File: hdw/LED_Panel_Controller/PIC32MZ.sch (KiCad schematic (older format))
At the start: 3 parts

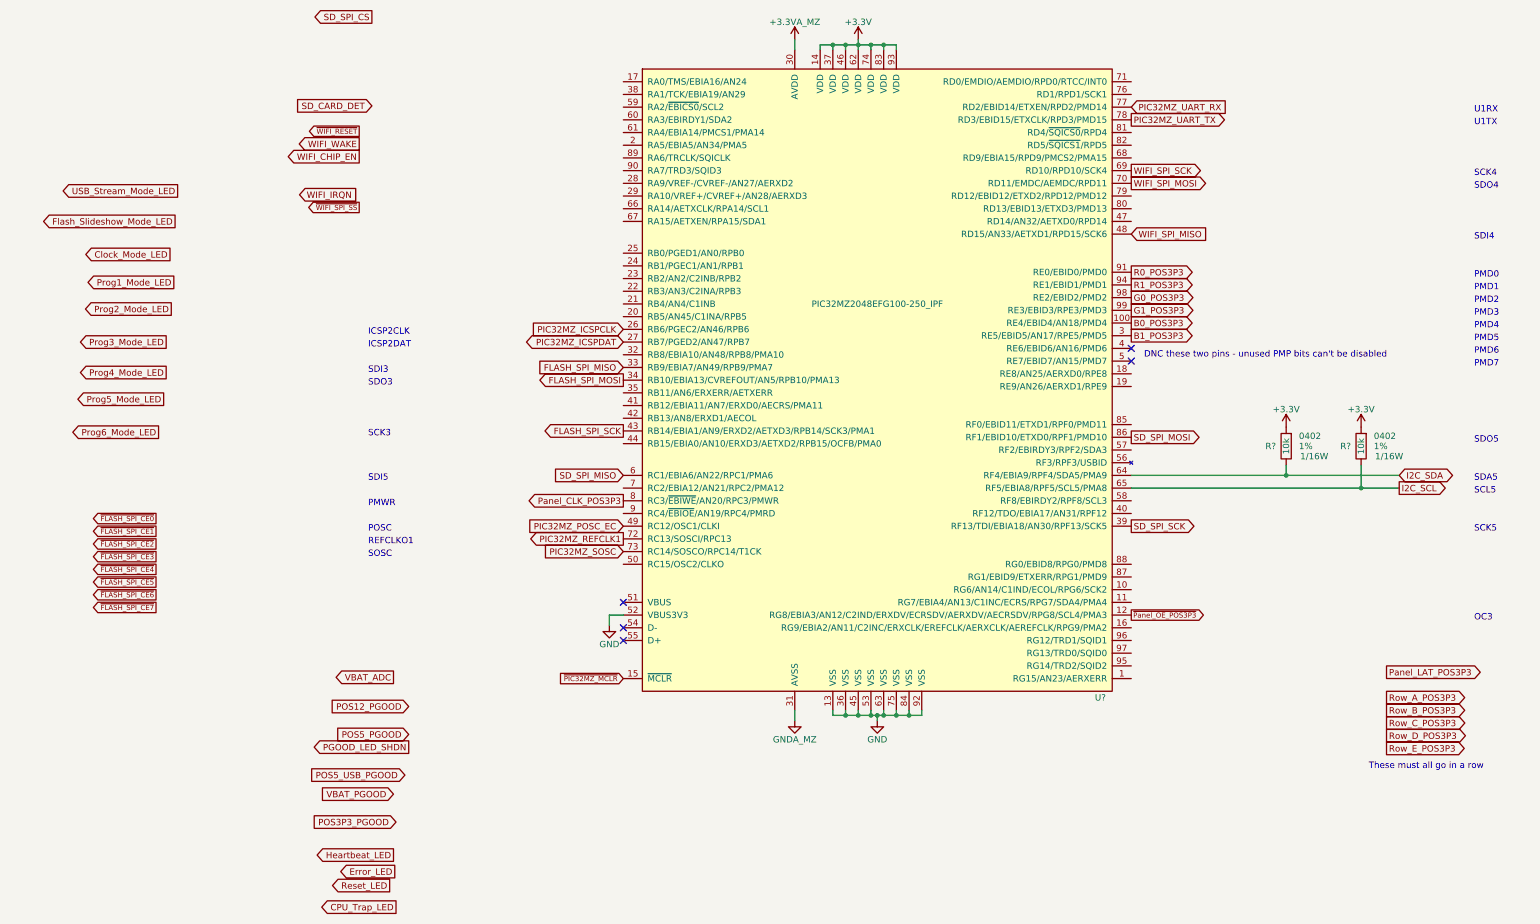
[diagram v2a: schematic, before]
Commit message: assigned a lot of nets to MCU pins
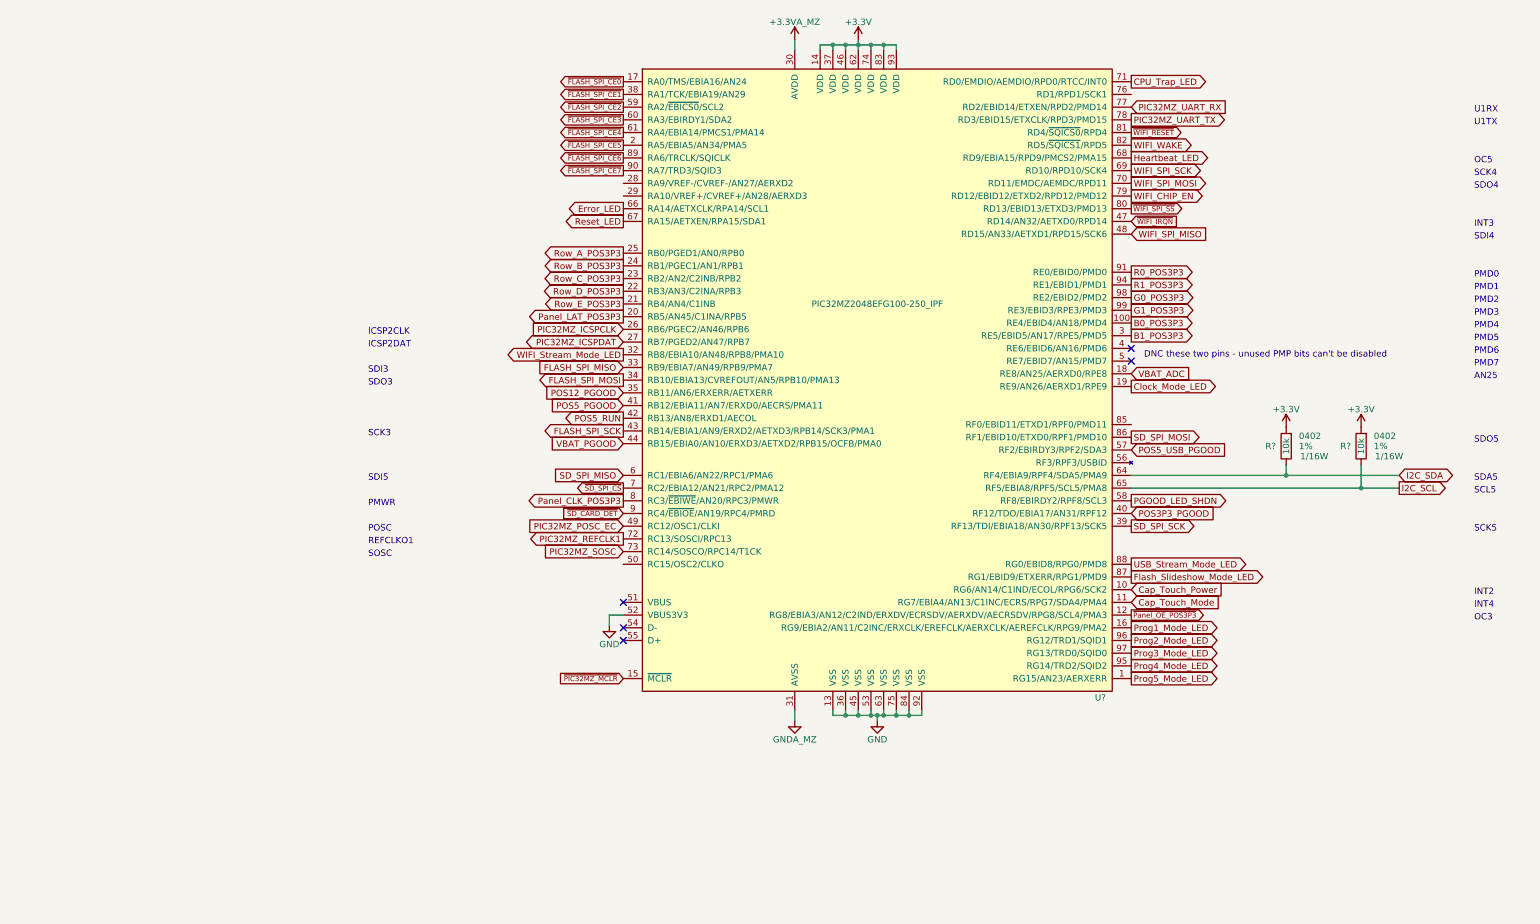
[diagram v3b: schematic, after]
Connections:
- net CPU_Trap_LED: now also U?.71 (RD0/EMDIO/AEMDIO/RPD0/RTCC/INT0)
- net Clock_Mode_LED: now also U?.19 (RE9/AN26/AERXD1/RPE9)
- net Error_LED: now also U?.66 (RA14/AETXCLK/RPA14/SCL1)
- net Flash_Slideshow_Mode_LED: now also U?.87 (RG1/EBID9/ETXERR/RPG1/PMD9)
- net Heartbeat_LED: now also U?.68 (RD9/EBIA15/RPD9/PMCS2/PMA15)
- net PGOOD_LED_SHDN: now also U?.58 (RF8/EBIRDY2/RPF8/SCL3)
- net POS12_PGOOD: now also U?.35 (RB11/AN6/ERXERR/AETXERR)
- net POS3P3_PGOOD: now also U?.40 (RF12/TDO/EBIA17/AN31/RPF12)
- net POS5_PGOOD: now also U?.41 (RB12/EBIA11/AN7/ERXD0/AECRS/PMA11)
- net POS5_USB_PGOOD: now also U?.57 (RF2/EBIRDY3/RPF2/SDA3)
- net Panel_LAT_POS3P3: now also U?.20 (RB5/AN45/C1INA/RPB5)
- net Prog1_Mode_LED: now also U?.16 (RG9/EBIA2/AN11/C2INC/ERXCLK/EREFCLK/AERXCLK/AEREFCLK/RPG9/PMA2)
- net Prog2_Mode_LED: now also U?.96 (RG12/TRD1/SQID1)
- net Prog3_Mode_LED: now also U?.97 (RG13/TRD0/SQID0)
- net Prog4_Mode_LED: now also U?.95 (RG14/TRD2/SQID2)
- net Prog5_Mode_LED: now also U?.1 (RG15/AN23/AERXERR)
- net Reset_LED: now also U?.67 (RA15/AETXEN/RPA15/SDA1)
- net Row_A_POS3P3: now also U?.25 (RB0/PGED1/AN0/RPB0)
- net Row_B_POS3P3: now also U?.24 (RB1/PGEC1/AN1/RPB1)
- net Row_C_POS3P3: now also U?.23 (RB2/AN2/C2INB/RPB2)
- net Row_D_POS3P3: now also U?.22 (RB3/AN3/C2INA/RPB3)
- net Row_E_POS3P3: now also U?.21 (RB4/AN4/C1INB)
- net USB_Stream_Mode_LED: now also U?.88 (RG0/EBID8/RPG0/PMD8)
- net VBAT_ADC: now also U?.18 (RE8/AN25/AERXD0/RPE8)
- net VBAT_PGOOD: now also U?.44 (RB15/EBIA0/AN10/ERXD3/AETXD2/RPB15/OCFB/PMA0)
- net WIFI_CHIP_EN: now also U?.79 (RD12/EBID12/ETXD2/RPD12/PMD12)
- net WIFI_WAKE: now also U?.82 (RD5/~SQICS1~/RPD5)
- net ~FLASH_SPI_CE0: now also U?.17 (RA0/TMS/EBIA16/AN24)
- net ~FLASH_SPI_CE1: now also U?.38 (RA1/TCK/EBIA19/AN29)
- net ~FLASH_SPI_CE2: now also U?.59 (RA2/~EBICS0~/SCL2)
- net ~FLASH_SPI_CE3: now also U?.60 (RA3/EBIRDY1/SDA2)
- net ~FLASH_SPI_CE4: now also U?.61 (RA4/EBIA14/PMCS1/PMA14)
- net ~FLASH_SPI_CE5: now also U?.2 (RA5/EBIA5/AN34/PMA5)
- net ~FLASH_SPI_CE6: now also U?.89 (RA6/TRCLK/SQICLK)
- net ~FLASH_SPI_CE7: now also U?.90 (RA7/TRD3/SQID3)
- net ~WIFI_RESET: now also U?.81 (RD4/~SQICS0~/RPD4)
- net ~WIFI_SPI_SS: now also U?.80 (RD13/EBID13/ETXD3/PMD13)
- net Cap_Touch_Power: now reaches U?.10 (RG6/AN14/C1IND/ECOL/RPG6/SCK2)
- net Cap_Touch_Mode: now reaches U?.11 (RG7/EBIA4/AN13/C1INC/ECRS/RPG7/SDA4/PMA4)
- net WIFI_Stream_Mode_LED: now reaches U?.32 (RB8/EBIA10/AN48/RPB8/PMA10)
- net POS5_RUN: now reaches U?.42 (RB13/AN8/ERXD1/AECOL)
- net ~WIFI_IRQN: now reaches U?.47 (RD14/AN32/AETXD0/RPD14)
- net ~SD_SPI_CS: now reaches U?.7 (RC2/EBIA12/AN21/RPC2/PMA12)
- net ~SD_CARD_DET: now reaches U?.9 (RC4/~EBIOE~/AN19/RPC4/PMRD)
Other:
- note added: "AN25"
- note added: "INT2"
- note added: "INT3"
- note added: "INT4"
- note added: "OC5"
- note removed: "These must all go in a row"
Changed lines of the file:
@@
 Text GLabel 3300 4990 0    50   Input ~ 0
 PIC32MZ_SOSC
-Text GLabel 1220 1680 0    40   Output ~ 0
+Text GLabel 7300 1690 2    40   Output ~ 0
 ~WIFI_RESET
-Text GLabel 1220 1780 0    50   Output ~ 0
+Text GLabel 7300 1790 2    50   Output ~ 0
 WIFI_WAKE
-Text GLabel 1220 1880 0    50   Output ~ 0
+Text GLabel 7300 2190 2    50   Output ~ 0
 WIFI_CHIP_EN
 Text GLabel 7300 1990 2    50   Output ~ 0
 WIFI_SPI_SCK
-Text GLabel 1220 2280 0    40   Output ~ 0
+Text GLabel 7300 2290 2    40   Output ~ 0
 ~WIFI_SPI_SS
 Text GLabel 7300 2090 2    50   Output ~ 0
@@
 Text GLabel 7300 2490 2    50   Input ~ 0
 WIFI_SPI_MISO
-Text GLabel 750  2180 2    50   Input ~ 0
-WIFI_IRQN
+Text GLabel 7300 2390 2    40   Input ~ 0
+~WIFI_IRQN
 $Comp
 L Custom_Library:PIC32MZ2048EFG100_IPF U?
@@
 Text Notes 1290 5040 0    50   ~ 0
 SOSC
-Text GLabel 1320 780  0    50   Output ~ 0
-SD_SPI_CS
+Text GLabel 3300 4490 0    40   Output ~ 0
+~SD_SPI_CS
 Text GLabel 7300 4090 2    50   Output ~ 0
 SD_SPI_MOSI
@@
 Text GLabel 3300 4390 0    50   Input ~ 0
 SD_SPI_MISO
-Text GLabel 1320 1480 0    50   Input ~ 0
-SD_CARD_DET
+Text GLabel 3300 4690 0    40   Input ~ 0
+~SD_CARD_DET
 Text GLabel 3300 4040 0    50   Output ~ 0
 FLASH_SPI_SCK
@@
 Text Notes 10000 3340 0    50   ~ 0
 PMD5
-Text GLabel 9310 5940 2    50   Output ~ 0
+Text GLabel 3300 3140 0    50   Output ~ 0
 Panel_LAT_POS3P3
 Text GLabel 7300 5490 2    40   Output ~ 0
@@
 Text GLabel 3300 4590 0    50   Output ~ 0
 Panel_CLK_POS3P3
-Text GLabel 9310 6340 2    50   Output ~ 0
+Text GLabel 3300 2840 0    50   Output ~ 0
 Row_C_POS3P3
-Text GLabel 9310 6540 2    50   Output ~ 0
+Text GLabel 3300 3040 0    50   Output ~ 0
 Row_E_POS3P3
-Text GLabel 9310 6440 2    50   Output ~ 0
+Text GLabel 3300 2940 0    50   Output ~ 0
 Row_D_POS3P3
-Text GLabel 9310 6240 2    50   Output ~ 0
+Text GLabel 3300 2740 0    50   Output ~ 0
 Row_B_POS3P3
-Text GLabel 9310 6140 2    50   Output ~ 0
+Text GLabel 3300 2640 0    50   Output ~ 0
 Row_A_POS3P3
 Text Notes 1290 4640 0    50   ~ 0
@@
 Text Notes 10000 5540 0    50   ~ 0
 OC3
-Text Notes 9170 6710 0    50   ~ 0
-These must all go in a row
 Text Notes 1290 4090 0    50   ~ 0
 SCK3
@@
 Text Notes 10000 4140 0    50   ~ 0
 SDO5
-Text GLabel 1610 6210 0    50   Input ~ 0
+Text GLabel 3300 3740 0    50   Input ~ 0
 POS12_PGOOD
-Text GLabel 1610 6430 0    50   Input ~ 0
+Text GLabel 3300 3840 0    50   Input ~ 0
 POS5_PGOOD
-Text GLabel 1610 6530 0    50   Output ~ 0
+Text GLabel 7300 4590 2    50   Output ~ 0
 PGOOD_LED_SHDN
-Text GLabel 1510 7120 0    50   Input ~ 0
+Text GLabel 7300 4690 2    50   Input ~ 0
 POS3P3_PGOOD
-Text GLabel 1490 6900 0    50   Input ~ 0
+Text GLabel 3300 4140 0    50   Input ~ 0
 VBAT_PGOOD
-Text GLabel 1580 6750 0    50   Input ~ 0
+Text GLabel 7300 4190 2    50   Input ~ 0
 POS5_USB_PGOOD
-Text GLabel 1490 7380 0    50   Output ~ 0
+Text GLabel 7300 1890 2    50   Output ~ 0
 Heartbeat_LED
-Text GLabel 1460 7620 0    50   Output ~ 0
+Text GLabel 3300 2390 0    50   Output ~ 0
 Reset_LED
-Text GLabel 1500 7510 0    50   Output ~ 0
+Text GLabel 3300 2290 0    50   Output ~ 0
 Error_LED
-Text GLabel 1510 7790 0    50   Output ~ 0
+Text GLabel 7300 1290 2    50   Output ~ 0
 CPU_Trap_LED
-Text GLabel 1490 5980 0    50   Output ~ 0
+Text GLabel 7300 3590 2    50   Input ~ 0
 VBAT_ADC
-Text GLabel -210 2150 0    50   Output ~ 0
+Text GLabel 7300 5090 2    50   Output ~ 0
 USB_Stream_Mode_LED
-Text GLabel -240 2870 0    50   Output ~ 0
+Text GLabel 7300 5590 2    50   Output ~ 0
 Prog1_Mode_LED
-Text GLabel -300 3580 0    50   Output ~ 0
+Text GLabel 7300 5890 2    50   Output ~ 0
 Prog4_Mode_LED
-Text GLabel -230 2390 0    50   Output ~ 0
+Text GLabel 7300 5190 2    50   Output ~ 0
 Flash_Slideshow_Mode_LED
-Text GLabel -260 3080 0    50   Output ~ 0
+Text GLabel 7300 5690 2    50   Output ~ 0
 Prog2_Mode_LED
-Text GLabel -320 3790 0    50   Output ~ 0
+Text GLabel 7300 5990 2    50   Output ~ 0
 Prog5_Mode_LED
-Text GLabel -300 3340 0    50   Output ~ 0
+Text GLabel 7300 5790 2    50   Output ~ 0
 Prog3_Mode_LED
-Text GLabel -360 4050 0    50   Output ~ 0
-Prog6_Mode_LED
-Text GLabel -270 2650 0    50   Output ~ 0
+Text GLabel 7300 3690 2    50   Output ~ 0
 Clock_Mode_LED
-Text GLabel -380 4730 0    40   Output ~ 0
+Text GLabel 3300 1290 0    40   Output ~ 0
 ~FLASH_SPI_CE0
-Text GLabel -380 4830 0    40   Output ~ 0
+Text GLabel 3300 1390 0    40   Output ~ 0
 ~FLASH_SPI_CE1
-Text GLabel -380 4930 0    40   Output ~ 0
+Text GLabel 3300 1490 0    40   Output ~ 0
 ~FLASH_SPI_CE2
-Text GLabel -380 5030 0    40   Output ~ 0
+Text GLabel 3300 1590 0    40   Output ~ 0
 ~FLASH_SPI_CE3
-Text GLabel -380 5130 0    40   Output ~ 0
+Text GLabel 3300 1690 0    40   Output ~ 0
 ~FLASH_SPI_CE4
-Text GLabel -380 5230 0    40   Output ~ 0
+Text GLabel 3300 1790 0    40   Output ~ 0
 ~FLASH_SPI_CE5
-Text GLabel -380 5330 0    40   Output ~ 0
+Text GLabel 3300 1890 0    40   Output ~ 0
 ~FLASH_SPI_CE6
-Text GLabel -380 5430 0    40   Output ~ 0
+Text GLabel 3300 1990 0    40   Output ~ 0
 ~FLASH_SPI_CE7
+Text GLabel 3300 3440 0    50   Output ~ 0
+WIFI_Stream_Mode_LED
+Text Notes 10000 1940 0    50   ~ 0
+OC5
+Text Notes 10000 3640 0    50   ~ 0
+AN25
+Text GLabel 7300 5290 2    50   Input ~ 0
+Cap_Touch_Power
+Text GLabel 7300 5390 2    50   Input ~ 0
+Cap_Touch_Mode
+Text Notes 10000 2440 0    50   ~ 0
+INT3
+Text Notes 10000 5340 0    50   ~ 0
+INT2
+Text Notes 10000 5440 0    50   ~ 0
+INT4
+Text GLabel 3300 3940 0    50   Output ~ 0
+POS5_RUN
 $EndSCHEMATC

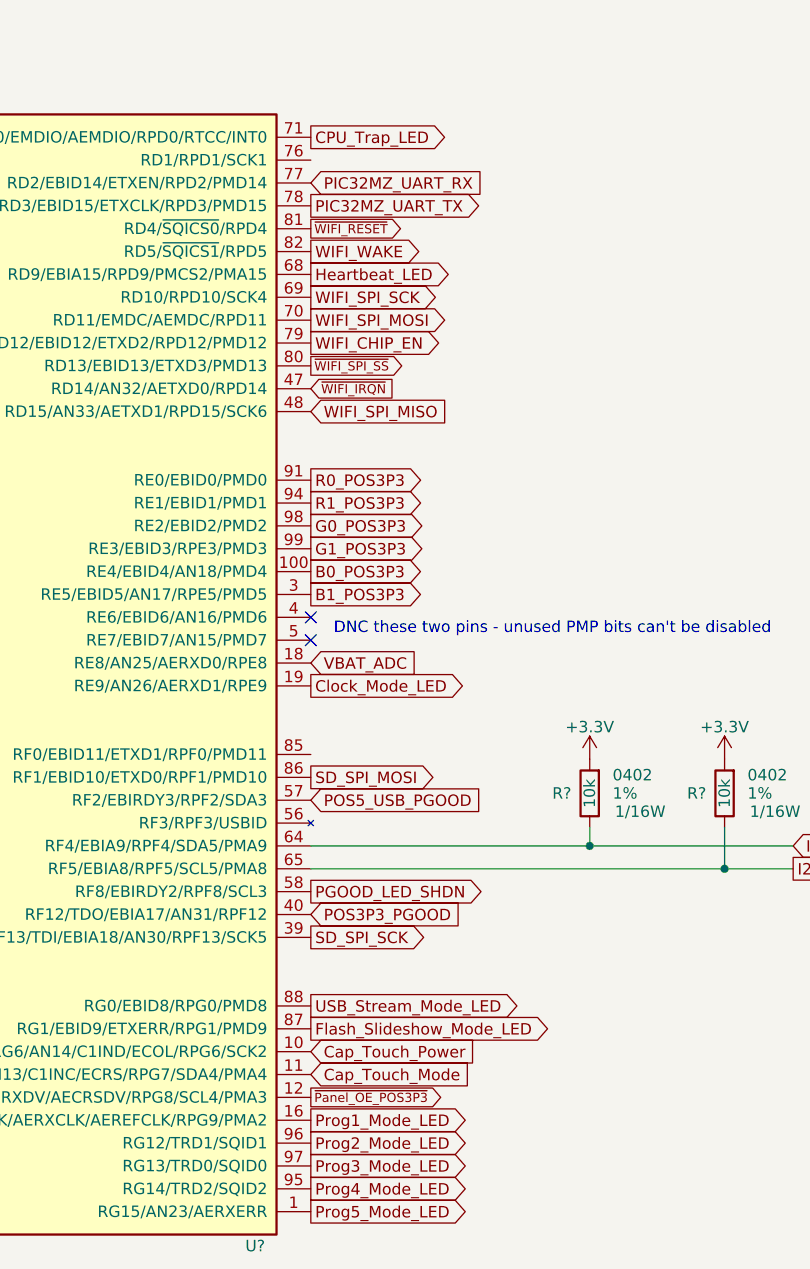
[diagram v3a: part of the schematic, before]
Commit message: Added panel dimming OR gate
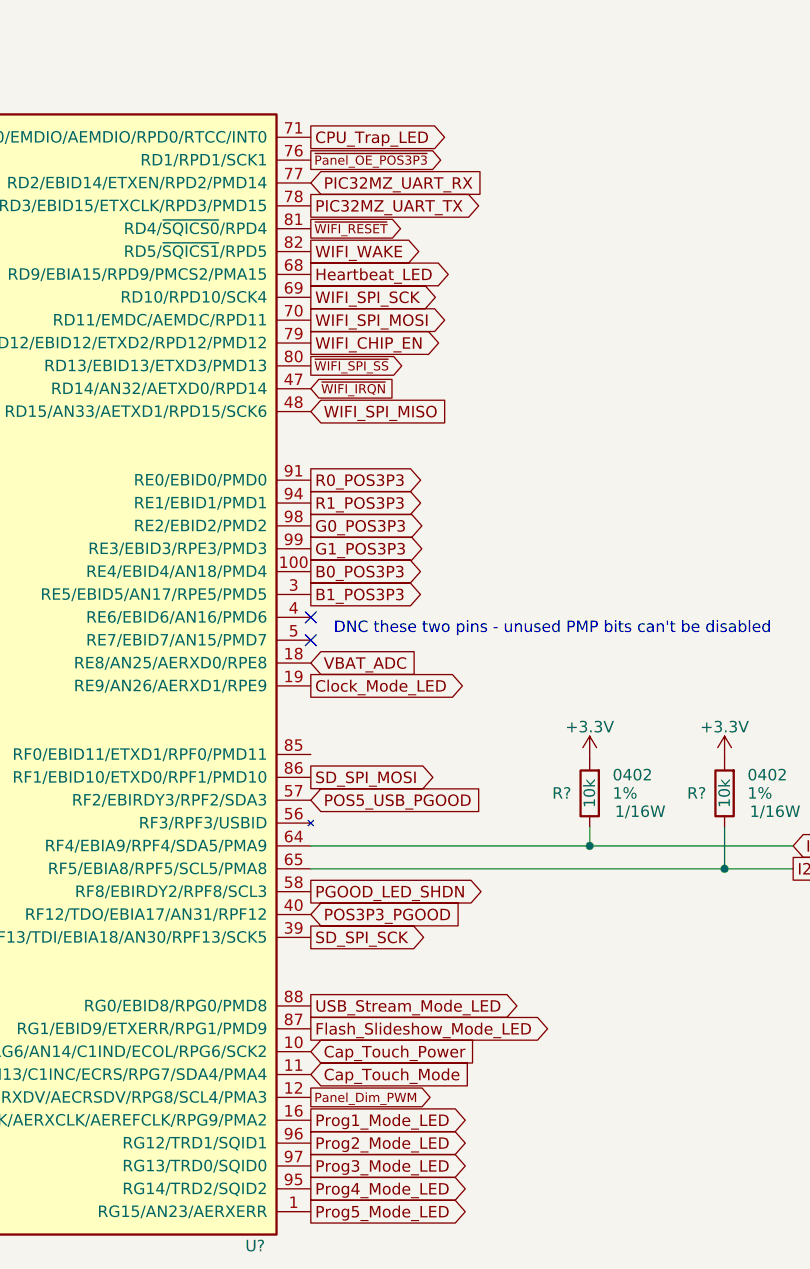
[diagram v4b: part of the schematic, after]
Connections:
- net ~Panel_OE_POS3P3: now also U?.76 (RD1/RPD1/SCK1); no longer U?.12 (RG8/EBIA3/AN12/C2IND/ERXDV/ECRSDV/AERXDV/AECRSDV/RPG8/SCL4/PMA3)
- new net Panel_Dim_PWM: U?.12 (RG8/EBIA3/AN12/C2IND/ERXDV/ECRSDV/AERXDV/AECRSDV/RPG8/SCL4/PMA3)
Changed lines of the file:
@@
 Panel_LAT_POS3P3
 Text GLabel 7300 5490 2    40   Output ~ 0
-~Panel_OE_POS3P3
+Panel_Dim_PWM
 Text GLabel 3300 4590 0    50   Output ~ 0
 Panel_CLK_POS3P3
@@
 Text GLabel 3300 3940 0    50   Output ~ 0
 POS5_RUN
+Text GLabel 7300 1390 2    40   Output ~ 0
+~Panel_OE_POS3P3
 $EndSCHEMATC
